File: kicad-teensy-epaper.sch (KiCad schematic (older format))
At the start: 18 parts, among them J1 TEENSY3.2-72MHz, J2 HEADER-FEMALE-34POS-FFC-SMT-1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, Q1 Q_NMOS_GDS

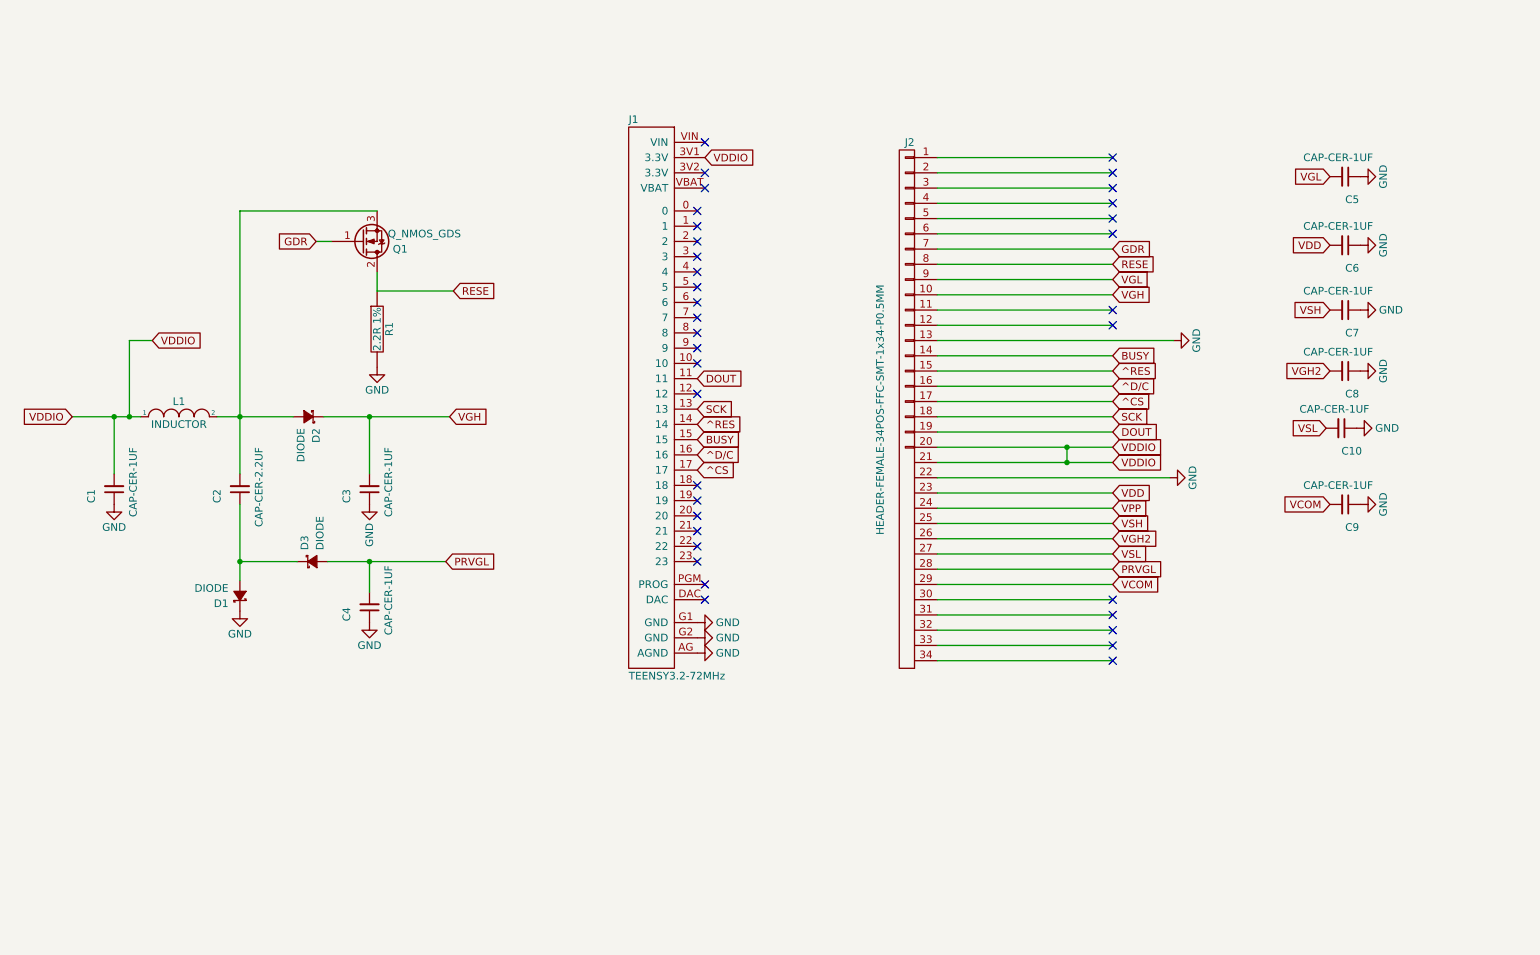
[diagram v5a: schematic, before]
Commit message: redesigned for smaller size and cap touch
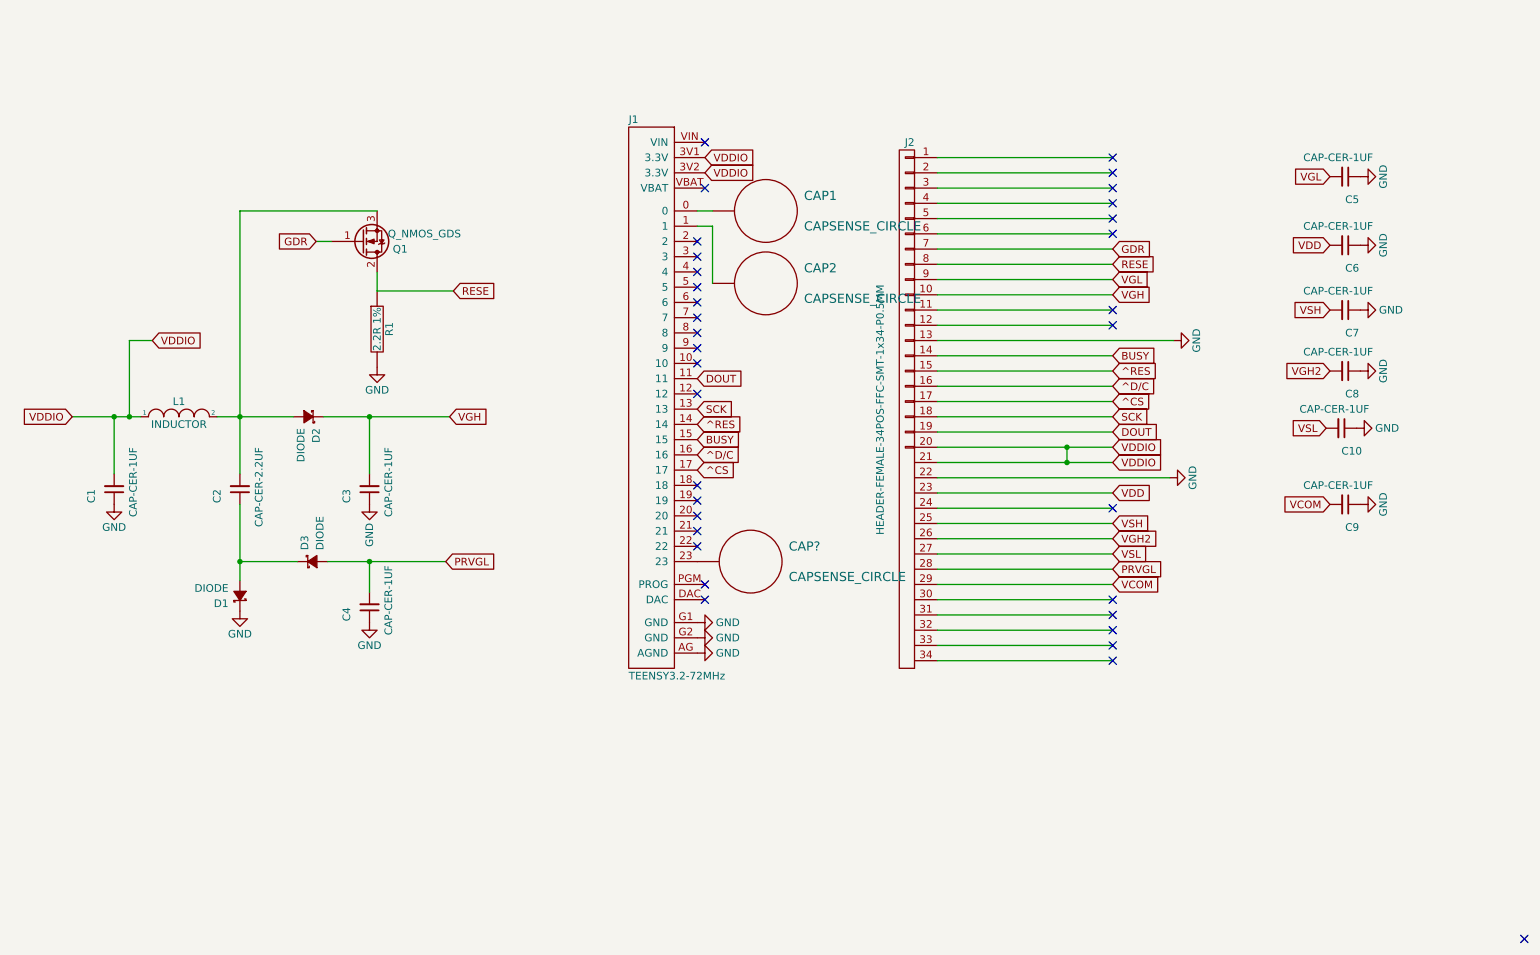
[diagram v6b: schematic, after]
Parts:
- added CAP1, CAP2, CAP?: CAPSENSE_CIRCLE, Wickerlib:CAPSENSE-CIRCLE-D10MM, symbol CAPSENSE_CIRCLE
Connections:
- net VDDIO: now also J1.3V2 (3.3V)
- net at J1.0: now also CAP1.1 (BUTTON)
- net at J1.1: now also CAP2.1 (BUTTON)
- net at J1.23: now also CAP?.1 (BUTTON)
- net VPP: no longer names the net of J2.24
- no-connect marks 36 -> 34
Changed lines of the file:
@@
 EESchema Schematic File Version 2
-LIBS:kicad-teensy-epaper-rescue
 LIBS:bbd
 LIBS:battery_management
@@
 Text GLabel 7775 3775 2    50   Input ~ 0
 VDD
-Text GLabel 7775 3875 2    50   Input ~ 0
-VPP
 Text GLabel 7775 3975 2    50   Input ~ 0
 VSH
@@
 Text GLabel 5050 3025 2    50   Input ~ 0
 DOUT
-NoConn ~ 5050 1925
-NoConn ~ 5050 2025
 NoConn ~ 5050 2125
 NoConn ~ 5050 2225
@@
 NoConn ~ 5050 3925
 NoConn ~ 5050 4025
-NoConn ~ 5050 4125
-NoConn ~ 5050 4225
 NoConn ~ 5100 4375
 NoConn ~ 5100 4475
@@
 $EndComp
 NoConn ~ 5100 1475
-NoConn ~ 5100 1675
 NoConn ~ 5100 1775
 Wire Wire Line
@@
 NoConn ~ 7775 2575
 NoConn ~ 7775 2675
+Text GLabel 5100 1675 2    50   Input ~ 0
+VDDIO
+$Comp
+L CAPSENSE_CIRCLE CAP1
+U 1 1 58FFF9C2
+P 5500 1925
+F 0 "CAP1" H 5750 2025 60  0000 L CNN
+F 1 "CAPSENSE_CIRCLE" H 5750 1825 60  0000 L CNN
+F 2 "Wickerlib:CAPSENSE-CIRCLE-D10MM" H 5500 1925 60  0001 C CNN
+F 3 "" H 5500 1925 60  0000 C CNN
+	1    5500 1925
+	1    0    0    -1
+$EndComp
+$Comp
+L CAPSENSE_CIRCLE CAP2
+U 1 1 58FFFBB1
+P 5500 2400
+F 0 "CAP2" H 5750 2500 60  0000 L CNN
+F 1 "CAPSENSE_CIRCLE" H 5750 2300 60  0000 L CNN
+F 2 "Wickerlib:CAPSENSE-CIRCLE-D10MM" H 5500 2400 60  0001 C CNN
+F 3 "" H 5500 2400 60  0000 C CNN
+	1    5500 2400
+	1    0    0    -1
+$EndComp
+Wire Wire Line
+	5050 1925 5150 1925
+Wire Wire Line
+	5050 2025 5150 2025
+Wire Wire Line
+	5150 2025 5150 2400
+NoConn ~ 7775 3875
+NoConn ~ 10475 6700
+NoConn ~ 5050 4125
+$Comp
+L CAPSENSE_CIRCLE CAP?
+U 1 1 590025D6
+P 5400 4225
+F 0 "CAP?" H 5650 4325 60  0000 L CNN
+F 1 "CAPSENSE_CIRCLE" H 5650 4125 60  0000 L CNN
+F 2 "Wickerlib:CAPSENSE-CIRCLE-D10MM" H 5400 4225 60  0001 C CNN
+F 3 "" H 5400 4225 60  0000 C CNN
+	1    5400 4225
+	1    0    0    -1
+$EndComp
 $EndSCHEMATC

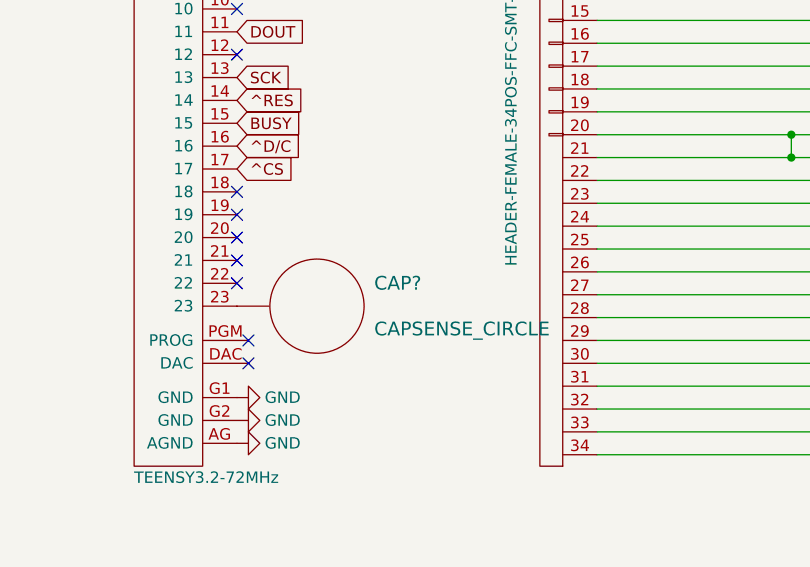
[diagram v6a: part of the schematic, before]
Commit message: update schematic
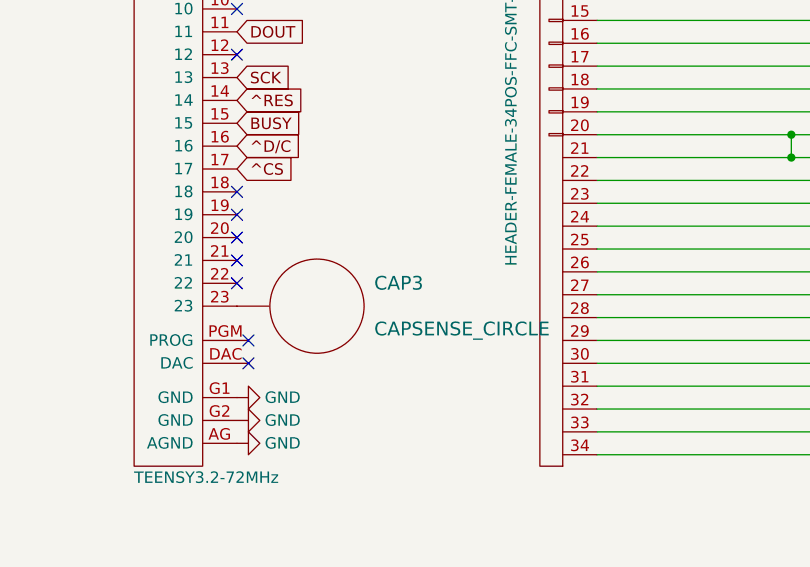
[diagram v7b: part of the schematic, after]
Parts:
- gave numbers to parts that had none: 1
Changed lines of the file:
@@
 VCOM
 $Comp
-L GND #PWR01
+L GND #PWR10
 U 1 1 5893E9A4
 P 8175 2775
-F 0 "#PWR01" H 8175 2525 50  0001 C CNN
+F 0 "#PWR10" H 8175 2525 50  0001 C CNN
 F 1 "GND" H 8175 2625 50  0000 C CNN
 F 2 "" H 8175 2775 50  0000 C CNN
@@
 $EndComp
 $Comp
-L GND #PWR02
+L GND #PWR12
 U 1 1 58941B65
 P 9400 1700
-F 0 "#PWR02" H 9400 1450 50  0001 C CNN
+F 0 "#PWR12" H 9400 1450 50  0001 C CNN
 F 1 "GND" H 9400 1550 50  0000 C CNN
 F 2 "" H 9400 1700 50  0000 C CNN
@@
 $EndComp
 $Comp
-L GND #PWR03
+L GND #PWR16
 U 1 1 58941CF9
 P 9400 3850
-F 0 "#PWR03" H 9400 3600 50  0001 C CNN
+F 0 "#PWR16" H 9400 3600 50  0001 C CNN
 F 1 "GND" H 9400 3700 50  0000 C CNN
 F 2 "" H 9400 3850 50  0000 C CNN
@@
 $EndComp
 $Comp
-L GND #PWR04
+L GND #PWR2
 U 1 1 58941E39
 P 2050 4550
-F 0 "#PWR04" H 2050 4300 50  0001 C CNN
+F 0 "#PWR2" H 2050 4300 50  0001 C CNN
 F 1 "GND" H 2050 4400 50  0000 C CNN
 F 2 "" H 2050 4550 50  0000 C CNN
@@
 $EndComp
 $Comp
-L GND #PWR05
+L GND #PWR1
 U 1 1 58941E7A
 P 1225 3850
-F 0 "#PWR05" H 1225 3600 50  0001 C CNN
+F 0 "#PWR1" H 1225 3600 50  0001 C CNN
 F 1 "GND" H 1225 3700 50  0000 C CNN
 F 2 "" H 1225 3850 50  0000 C CNN
@@
 $EndComp
 $Comp
-L GND #PWR06
+L GND #PWR5
 U 1 1 58941EFC
 P 2950 2950
-F 0 "#PWR06" H 2950 2700 50  0001 C CNN
+F 0 "#PWR5" H 2950 2700 50  0001 C CNN
 F 1 "GND" H 2950 2800 50  0000 C CNN
 F 2 "" H 2950 2950 50  0000 C CNN
@@
 Connection ~ 1225 3275
 $Comp
-L GND #PWR07
+L GND #PWR13
 U 1 1 58952731
 P 9400 2150
-F 0 "#PWR07" H 9400 1900 50  0001 C CNN
+F 0 "#PWR13" H 9400 1900 50  0001 C CNN
 F 1 "GND" H 9400 2000 50  0000 C CNN
 F 2 "" H 9400 2150 50  0000 C CNN
@@
 $EndComp
 $Comp
-L GND #PWR08
+L GND #PWR6
 U 1 1 58953BD1
 P 5050 4625
-F 0 "#PWR08" H 5050 4375 50  0001 C CNN
+F 0 "#PWR6" H 5050 4375 50  0001 C CNN
 F 1 "GND" V 5050 4425 50  0000 C CNN
 F 2 "" H 5050 4625 50  0000 C CNN
@@
 $EndComp
 $Comp
-L GND #PWR09
+L GND #PWR15
 U 1 1 58953E27
 P 9400 2975
-F 0 "#PWR09" H 9400 2725 50  0001 C CNN
+F 0 "#PWR15" H 9400 2725 50  0001 C CNN
 F 1 "GND" H 9400 2825 50  0000 C CNN
 F 2 "" H 9400 2975 50  0000 C CNN
@@
 $EndComp
 $Comp
-L GND #PWR010
+L GND #PWR4
 U 1 1 58954CBF
 P 2900 4625
-F 0 "#PWR010" H 2900 4375 50  0001 C CNN
+F 0 "#PWR4" H 2900 4375 50  0001 C CNN
 F 1 "GND" H 2900 4475 50  0000 C CNN
 F 2 "" H 2900 4625 50  0000 C CNN
@@
 $EndComp
 $Comp
-L GND #PWR011
+L GND #PWR14
 U 1 1 58954E61
 P 9400 2575
-F 0 "#PWR011" H 9400 2325 50  0001 C CNN
+F 0 "#PWR14" H 9400 2325 50  0001 C CNN
 F 1 "GND" V 9400 2375 50  0000 C CNN
 F 2 "" H 9400 2575 50  0000 C CNN
@@
 $EndComp
 $Comp
-L GND #PWR012
+L GND #PWR3
 U 1 1 58955108
 P 2900 3850
-F 0 "#PWR012" H 2900 3600 50  0001 C CNN
+F 0 "#PWR3" H 2900 3600 50  0001 C CNN
 F 1 "GND" V 2900 3650 50  0000 C CNN
 F 2 "" H 2900 3850 50  0000 C CNN
@@
 VSL
 $Comp
-L GND #PWR013
+L GND #PWR11
 U 1 1 589557C5
 P 9375 3350
-F 0 "#PWR013" H 9375 3100 50  0001 C CNN
+F 0 "#PWR11" H 9375 3100 50  0001 C CNN
 F 1 "GND" V 9375 3150 50  0000 C CNN
 F 2 "" H 9375 3350 50  0000 C CNN
@@
 $EndComp
 $Comp
-L GND #PWR014
+L GND #PWR8
 U 1 1 58956AE7
 P 5050 4825
-F 0 "#PWR014" H 5050 4575 50  0001 C CNN
+F 0 "#PWR8" H 5050 4575 50  0001 C CNN
 F 1 "GND" V 5050 4625 50  0000 C CNN
 F 2 "" H 5050 4825 50  0000 C CNN
@@
 $EndComp
 $Comp
-L GND #PWR015
+L GND #PWR7
 U 1 1 58956B28
 P 5050 4725
-F 0 "#PWR015" H 5050 4475 50  0001 C CNN
+F 0 "#PWR7" H 5050 4475 50  0001 C CNN
 F 1 "GND" V 5050 4525 50  0000 C CNN
 F 2 "" H 5050 4725 50  0000 C CNN
@@
 NoConn ~ 7775 4875
 $Comp
-L GND #PWR016
+L GND #PWR9
 U 1 1 58DB75A7
 P 8150 3675
-F 0 "#PWR016" H 8150 3425 50  0001 C CNN
+F 0 "#PWR9" H 8150 3425 50  0001 C CNN
 F 1 "GND" H 8150 3525 50  0000 C CNN
 F 2 "" H 8150 3675 50  0000 C CNN
@@
 NoConn ~ 5050 4125
 $Comp
-L CAPSENSE_CIRCLE CAP?
+L CAPSENSE_CIRCLE CAP3
 U 1 1 590025D6
 P 5400 4225
-F 0 "CAP?" H 5650 4325 60  0000 L CNN
+F 0 "CAP3" H 5650 4325 60  0000 L CNN
 F 1 "CAPSENSE_CIRCLE" H 5650 4125 60  0000 L CNN
 F 2 "Wickerlib:CAPSENSE-CIRCLE-D10MM" H 5400 4225 60  0001 C CNN
